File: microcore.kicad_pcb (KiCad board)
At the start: 4 copper layers, 90 x 76.6 mm, 21 parts, among them J1 TE_776231-1, J8 USB_B_Mini, M1 Module:mega-mcu100/0.3, M2 Module-power_12and5V-0.3, M3 Module-vr-max9924-0.3, Q1 VND14NV04-E, Q2 VND14NV04-E, Q3 VND14NV04-E, Q4 VND14NV04-E, Q5 VND14NV04-E, Q6 VND14NV04-E, Q7 VND14NV04-E

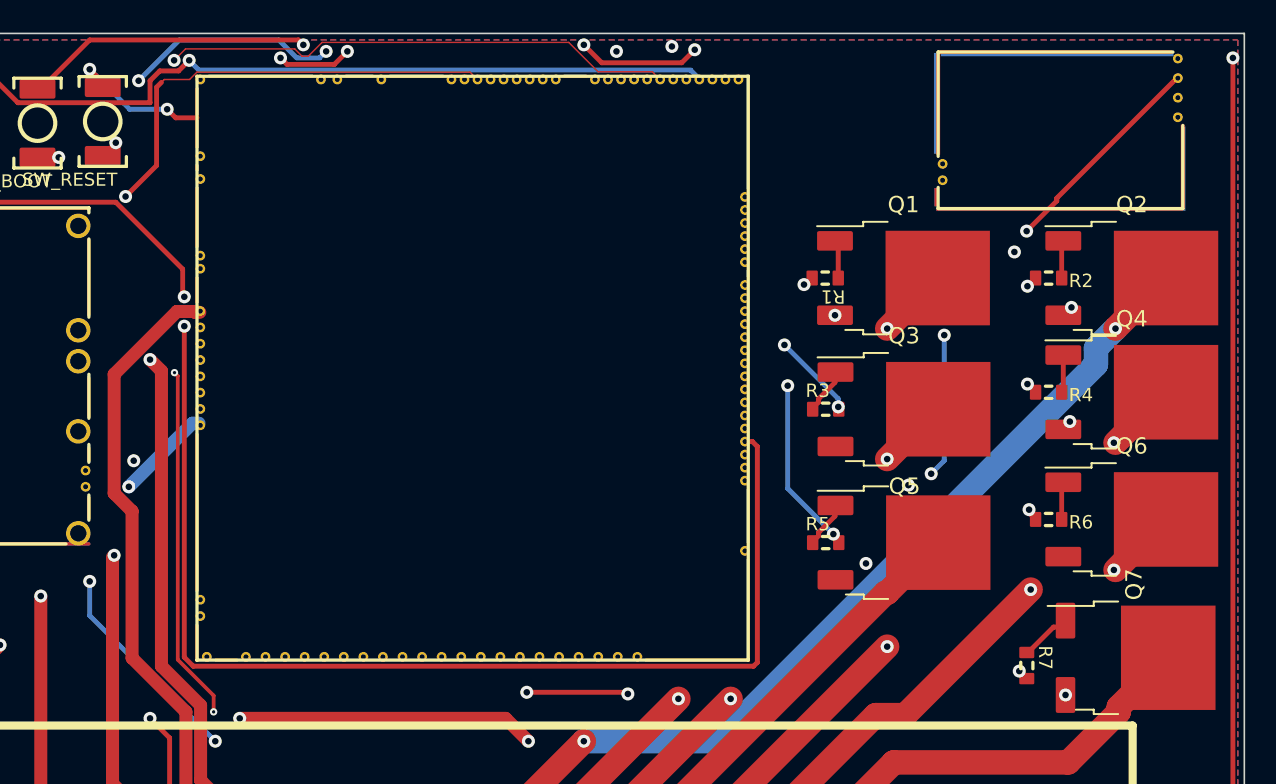
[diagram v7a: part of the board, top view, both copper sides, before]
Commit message: Rev j: injector SMAJ33A TVS, US1M flyback, and 2nd 12Ω per INJ channel
SPEC power-stage protection on INJ4 sch+PCB: R8–R11 ballast, D1–D4 US1M,
D5–D8 SMAJ33A (DO-214AC equivalent of SMBJ33A). FET cluster left in place;
new parts in alley + pocket C. BOARD_REVISION bumped to j. PCB remains
substantial (zones + aux origin intact).

Co-authored-by: Quintin <quintinbannink42@users.noreply.github.com>
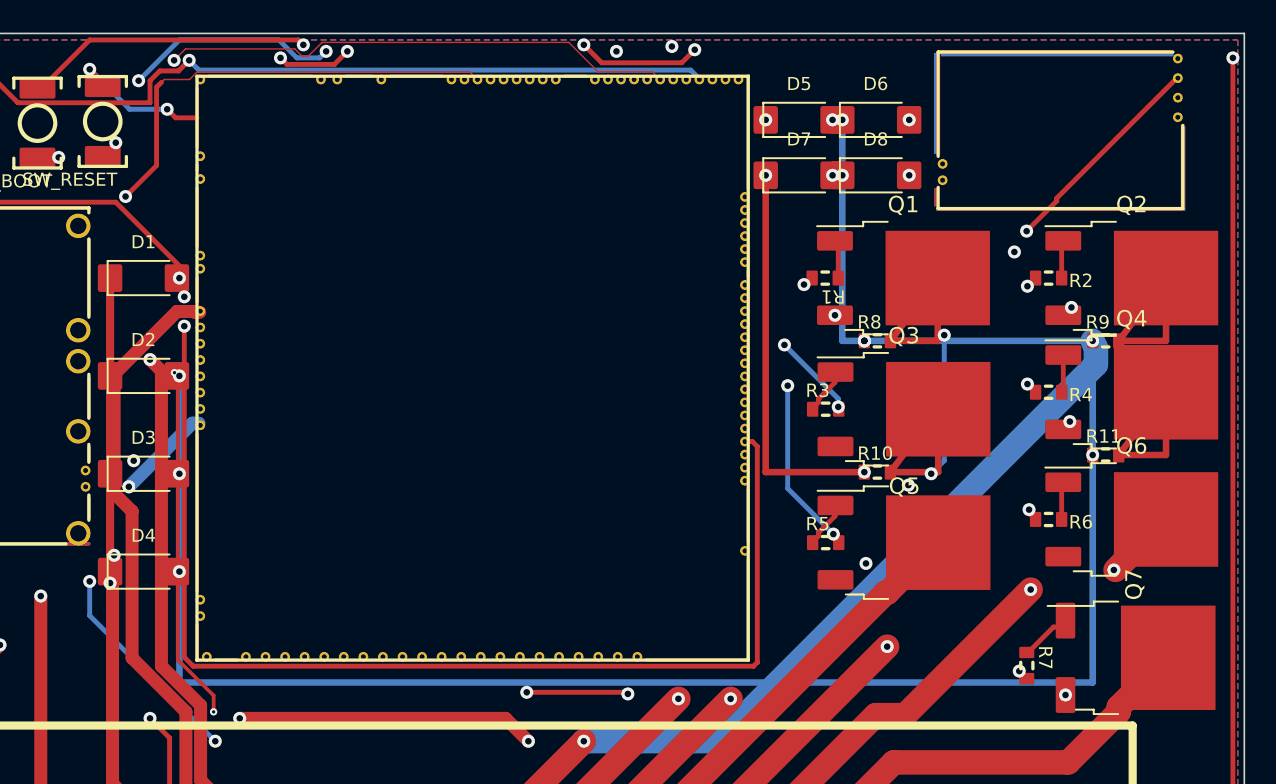
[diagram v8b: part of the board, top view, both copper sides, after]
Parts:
- added D1: US1M, DO214AC, F.Cu at (130.0, 86.5)
- added D2: US1M, DO214AC, F.Cu at (130.0, 92.5)
- added D3: US1M, DO214AC, F.Cu at (130.0, 98.5)
- added D4: US1M, DO214AC, F.Cu at (130.0, 104.5)
- added D5: SMAJ33A, DO214AC, F.Cu at (170.2, 76.8)
- added D6: SMAJ33A, DO214AC, F.Cu at (174.9, 76.8)
- added D7: SMAJ33A, DO214AC, F.Cu at (170.2, 80.2)
- added D8: SMAJ33A, DO214AC, F.Cu at (174.9, 80.2)
- added R10: 12, R0603, F.Cu at (175.0, 98.4)
- added R11: 12, R0603, F.Cu at (189.0, 97.3)
- added R8: 12, R0603, F.Cu at (175.0, 90.3)
- added R9: 12, R0603, F.Cu at (189.0, 90.3)
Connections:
- Q1 pad 2: /INJ1 -> Net-(Q1-D)
- Q2 pad 2: /INJ2 -> Net-(Q2-D)
- Q3 pad 2: /INJ3 -> Net-(Q3-D)
- Q4 pad 2: /INJ4 -> Net-(Q4-D)
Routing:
- net /INJ2: track 67.0 -> 186.2 mm, vias 3 -> 5
- net /INJ4: track 54.8 -> 161.4 mm, vias 3 -> 5
- net /INJ1: track 60.4 -> 160.6 mm, vias 2 -> 5
- net /INJ3: track 48.3 -> 136.7 mm, vias 3 -> 5
- net /V12_RAW: track 52.6 -> 87.8 mm, vias 2 -> 3
- net Net-(Q3-D): track 0.00 -> 11.7 mm
- net Net-(Q4-D): track 0.00 -> 11.6 mm
- net Net-(Q2-D): track 0.00 -> 11.6 mm
- net Net-(Q1-D): track 0.00 -> 11.6 mm
- net GND: vias 7 -> 11
